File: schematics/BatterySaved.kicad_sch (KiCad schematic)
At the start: 11 parts, among them Q1 2SA1015, Q2 2SC1815, U2 74LS32

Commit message: WIP
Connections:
- net BATYCC renamed BATV_CC
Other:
- note added: "14 pin: BAT_VCC"
- note removed: "14 pin: BATYCC"
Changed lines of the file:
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@@
     (fill (type none))
   )
-  (text "14 pin: BATYCC" (at 82.55 87.63 0)
+  (text "14 pin: BAT_VCC" (at 82.55 87.63 0)
     (effects (font (size 1.27 1.27)) (justify left bottom))
   )
@@
     )
   )
-  (global_label "BATYCC" (shape input) (at 102.87 46.99 0) (fields_autoplaced)
+  (global_label "BATV_CC" (shape output) (at 102.87 46.99 0) (fields_autoplaced)
     (effects (font (size 1.27 1.27)) (justify left))
-    (property "Intersheetrefs" "${INTERSHEET_REFS}" (at 112.81 46.99 0)
+    (property "Intersheetrefs" "${INTERSHEET_REFS}" (at 113.7776 46.99 0)
       (effects (font (size 1.27 1.27)) (justify left))
     )

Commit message: Complete pages 1-4
completion of pages 1 to 4
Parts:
- R1, R2, R3, R4: symbol Device:R_Small_US -> Device:R
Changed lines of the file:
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@@
     (comment 4 "NEO-GEO MVS MV1F")
   )
+  (junction (at 62.23 57.15) (diameter 0) (color 0 0 0 0)
+  )
   (junction (at 54.61 101.6) (diameter 0) (color 0 0 0 0)
   )
@@
   (junction (at 41.91 39.37) (diameter 0) (color 0 0 0 0)
   )
-  (junction (at 62.23 57.15) (diameter 0) (color 0 0 0 0)
-  )
   (junction (at 87.63 46.99) (diameter 0) (color 0 0 0 0)
   )
@@
     (stroke (width 0) (type default))
   )
-  (wire (pts (xy 72.39 46.99) (xy 72.39 49.53))
+  (wire (pts (xy 72.39 46.99) (xy 72.39 48.26))
     (stroke (width 0) (type default))
   )
@@
     (stroke (width 0) (type default))
   )
-  (wire (pts (xy 59.69 83.82) (xy 29.21 83.82))
+  (wire (pts (xy 29.21 83.82) (xy 58.42 83.82))
     (stroke (width 0) (type default))
   )
@@
     (stroke (width 0) (type default))
   )
-  (wire (pts (xy 41.91 39.37) (xy 45.72 39.37))
-    (stroke (width 0) (type default))
-  )
   (wire (pts (xy 73.66 113.03) (xy 76.2 113.03))
     (stroke (width 0) (type default))
   )
+  (wire (pts (xy 62.23 57.15) (xy 62.23 55.88))
+    (stroke (width 0) (type default))
+  )
   (wire (pts (xy 45.72 110.49) (xy 58.42 110.49))
     (stroke (width 0) (type default))
   )
+  (wire (pts (xy 87.63 46.99) (xy 72.39 46.99))
+    (stroke (width 0) (type default))
+  )
+  (wire (pts (xy 58.42 96.52) (xy 54.61 96.52))
+    (stroke (width 0) (type default))
+  )
+  (wire (pts (xy 76.2 99.06) (xy 83.82 99.06))
+    (stroke (width 0) (type default))
+  )
+  (wire (pts (xy 58.42 140.97) (xy 52.07 140.97))
+    (stroke (width 0) (type default))
+  )
+  (wire (pts (xy 73.66 129.54) (xy 83.82 129.54))
+    (stroke (width 0) (type default))
+  )
+  (wire (pts (xy 45.72 115.57) (xy 58.42 115.57))
+    (stroke (width 0) (type default))
+  )
+  (wire (pts (xy 41.91 39.37) (xy 41.91 46.99))
+    (stroke (width 0) (type default))
+  )
+  (wire (pts (xy 29.21 83.82) (xy 29.21 60.96))
+    (stroke (width 0) (type default))
+  )
+  (wire (pts (xy 52.07 39.37) (xy 54.61 39.37))
+    (stroke (width 0) (type default))
+  )
+  (wire (pts (xy 54.61 101.6) (xy 58.42 101.6))
+    (stroke (width 0) (type default))
+  )
+  (wire (pts (xy 76.2 120.65) (xy 52.07 120.65))
+    (stroke (width 0) (type default))
+  )
+  (wire (pts (xy 45.72 101.6) (xy 54.61 101.6))
+    (stroke (width 0) (type default))
+  )
+  (wire (pts (xy 87.63 46.99) (xy 87.63 59.69))
+    (stroke (width 0) (type default))
+  )
+  (wire (pts (xy 76.2 83.82) (xy 76.2 99.06))
+    (stroke (width 0) (type default))
+  )
   (wire (pts (xy 62.23 57.15) (xy 62.23 58.42))
     (stroke (width 0) (type default))
   )
-  (wire (pts (xy 87.63 46.99) (xy 72.39 46.99))
-    (stroke (width 0) (type default))
-  )
-  (wire (pts (xy 62.23 55.88) (xy 62.23 57.15))
-    (stroke (width 0) (type default))
-  )
-  (wire (pts (xy 58.42 96.52) (xy 54.61 96.52))
-    (stroke (width 0) (type default))
-  )
-  (wire (pts (xy 76.2 99.06) (xy 83.82 99.06))
-    (stroke (width 0) (type default))
-  )
-  (wire (pts (xy 58.42 140.97) (xy 52.07 140.97))
-    (stroke (width 0) (type default))
-  )
-  (wire (pts (xy 73.66 129.54) (xy 83.82 129.54))
-    (stroke (width 0) (type default))
-  )
-  (wire (pts (xy 45.72 115.57) (xy 58.42 115.57))
-    (stroke (width 0) (type default))
-  )
-  (wire (pts (xy 41.91 39.37) (xy 41.91 46.99))
-    (stroke (width 0) (type default))
-  )
-  (wire (pts (xy 29.21 83.82) (xy 29.21 60.96))
-    (stroke (width 0) (type default))
-  )
-  (wire (pts (xy 50.8 39.37) (xy 54.61 39.37))
-    (stroke (width 0) (type default))
-  )
-  (wire (pts (xy 54.61 101.6) (xy 58.42 101.6))
-    (stroke (width 0) (type default))
-  )
-  (wire (pts (xy 76.2 120.65) (xy 52.07 120.65))
-    (stroke (width 0) (type default))
-  )
-  (wire (pts (xy 45.72 101.6) (xy 54.61 101.6))
-    (stroke (width 0) (type default))
-  )
-  (wire (pts (xy 87.63 46.99) (xy 87.63 59.69))
-    (stroke (width 0) (type default))
-  )
-  (wire (pts (xy 76.2 83.82) (xy 76.2 99.06))
-    (stroke (width 0) (type default))
-  )
   (wire (pts (xy 52.07 140.97) (xy 52.07 127))
     (stroke (width 0) (type default))
@@
     (stroke (width 0) (type default))
   )
-  (wire (pts (xy 50.8 46.99) (xy 62.23 46.99))
+  (wire (pts (xy 52.07 46.99) (xy 62.23 46.99))
     (stroke (width 0) (type default))
   )
@@
     (stroke (width 0) (type default))
   )
-  (wire (pts (xy 41.91 46.99) (xy 45.72 46.99))
+  (wire (pts (xy 41.91 39.37) (xy 44.45 39.37))
+    (stroke (width 0) (type default))
+  )
+  (wire (pts (xy 41.91 46.99) (xy 44.45 46.99))
     (stroke (width 0) (type default))
   )
@@
     (stroke (width 0) (type default))
   )
-  (wire (pts (xy 76.2 83.82) (xy 64.77 83.82))
+  (wire (pts (xy 76.2 83.82) (xy 66.04 83.82))
     (stroke (width 0) (type default))
   )
@@
     (stroke (width 0) (type default))
   )
-  (wire (pts (xy 62.23 46.99) (xy 62.23 50.8))
+  (wire (pts (xy 62.23 46.99) (xy 62.23 48.26))
+    (stroke (width 0) (type default))
+  )
+  (wire (pts (xy 72.39 57.15) (xy 72.39 55.88))
     (stroke (width 0) (type default))
   )
@@
     )
   )
-  (symbol (lib_id "Device:R_Small_US") (at 62.23 53.34 180) (unit 1)
-    (in_bom yes) (on_board yes) (dnp no) (fields_autoplaced)
-    (property "Reference" "R3" (at 57.1967 53.34 90)
-      (effects (font (size 1.27 1.27)) hide)
-    )
-    (property "Value" "470" (at 63.881 53.34 0)
+  (symbol (lib_id "Device:R") (at 62.23 52.07 180) (unit 1)
+    (in_bom yes) (on_board yes) (dnp no) (fields_autoplaced)
+    (property "Reference" "R3" (at 57.1967 52.07 90)
+      (effects (font (size 1.27 1.27)) hide)
+    )
+    (property "Value" "470" (at 63.881 52.07 0)
       (effects (font (size 1.27 1.27)) (justify right))
     )
-    (property "Footprint" "" (at 62.23 53.34 0)
-      (effects (font (size 1.27 1.27)) hide)
-    )
-    (property "Datasheet" "~" (at 62.23 53.34 0)
+    (property "Footprint" "" (at 64.008 52.07 90)
+      (effects (font (size 1.27 1.27)) hide)
+    )
+    (property "Datasheet" "~" (at 62.23 52.07 0)
       (effects (font (size 1.27 1.27)) hide)
     )
@@
     )
   )
-  (symbol (lib_id "Device:R_Small_US") (at 62.23 83.82 90) (unit 1)
+  (symbol (lib_id "Device:R") (at 62.23 83.82 90) (unit 1)
     (in_bom yes) (on_board yes) (dnp no) (fields_autoplaced)
     (property "Reference" "R4" (at 62.23 78.7867 90)
@@
       (effects (font (size 1.27 1.27)))
     )
-    (property "Footprint" "" (at 62.23 83.82 0)
+    (property "Footprint" "" (at 62.23 85.598 90)
       (effects (font (size 1.27 1.27)) hide)
     )
@@
     )
   )
-  (symbol (lib_id "Diode:1N4001") (at 72.39 53.34 270) (unit 1)
-    (in_bom yes) (on_board yes) (dnp no) (fields_autoplaced)
-    (property "Reference" "D2" (at 70.358 54.5521 90)
+  (symbol (lib_id "Diode:1N4001") (at 72.39 52.07 270) (unit 1)
+    (in_bom yes) (on_board yes) (dnp no) (fields_autoplaced)
+    (property "Reference" "D2" (at 70.358 53.2821 90)
       (effects (font (size 1.27 1.27)) (justify right) hide)
     )
-    (property "Value" "1S1588" (at 74.422 53.34 90)
-      (effects (font (size 1.27 1.27)) (justify left))
-    )
-    (property "Footprint" "Diode_THT:D_DO-41_SOD81_P10.16mm_Horizontal" (at 72.39 53.34 0)
-      (effects (font (size 1.27 1.27)) hide)
-    )
-    (property "Datasheet" "http://www.vishay.com/docs/88503/1n4001.pdf" (at 72.39 53.34 0)
-      (effects (font (size 1.27 1.27)) hide)
-    )
-    (property "Sim.Device" "D" (at 72.39 53.34 0)
-      (effects (font (size 1.27 1.27)) hide)
-    )
-    (property "Sim.Pins" "1=K 2=A" (at 72.39 53.34 0)
+    (property "Value" "1S1588" (at 74.422 52.07 90)
+      (effects (font (size 1.27 1.27)) (justify left))
+    )
+    (property "Footprint" "Diode_THT:D_DO-41_SOD81_P10.16mm_Horizontal" (at 72.39 52.07 0)
+      (effects (font (size 1.27 1.27)) hide)
+    )
+    (property "Datasheet" "http://www.vishay.com/docs/88503/1n4001.pdf" (at 72.39 52.07 0)
+      (effects (font (size 1.27 1.27)) hide)
+    )
+    (property "Sim.Device" "D" (at 72.39 52.07 0)
+      (effects (font (size 1.27 1.27)) hide)
+    )
+    (property "Sim.Pins" "1=K 2=A" (at 72.39 52.07 0)
       (effects (font (size 1.27 1.27)) hide)
     )
@@
     )
   )
-  (symbol (lib_id "Device:R_Small_US") (at 48.26 39.37 90) (unit 1)
+  (symbol (lib_id "Device:R") (at 48.26 39.37 90) (unit 1)
     (in_bom yes) (on_board yes) (dnp no) (fields_autoplaced)
     (property "Reference" "R1" (at 48.26 34.3367 90)
@@
       (effects (font (size 1.27 1.27)))
     )
-    (property "Footprint" "" (at 48.26 39.37 0)
+    (property "Footprint" "" (at 48.26 41.148 90)
       (effects (font (size 1.27 1.27)) hide)
     )
@@
     )
   )
-  (symbol (lib_id "Device:R_Small_US") (at 48.26 46.99 90) (unit 1)
+  (symbol (lib_id "Device:R") (at 48.26 46.99 90) (unit 1)
     (in_bom yes) (on_board yes) (dnp no) (fields_autoplaced)
     (property "Reference" "R2" (at 48.26 41.9567 90)
@@
       (effects (font (size 1.27 1.27)))
     )
-    (property "Footprint" "" (at 48.26 46.99 0)
-      (effects (font (size 1.27 1.27)) hide)
-    )
+    (property "Footprint" "" (at 48.26 48.768 90)
+      (effects (font (size 1.27 1.27)) hide)
+    )

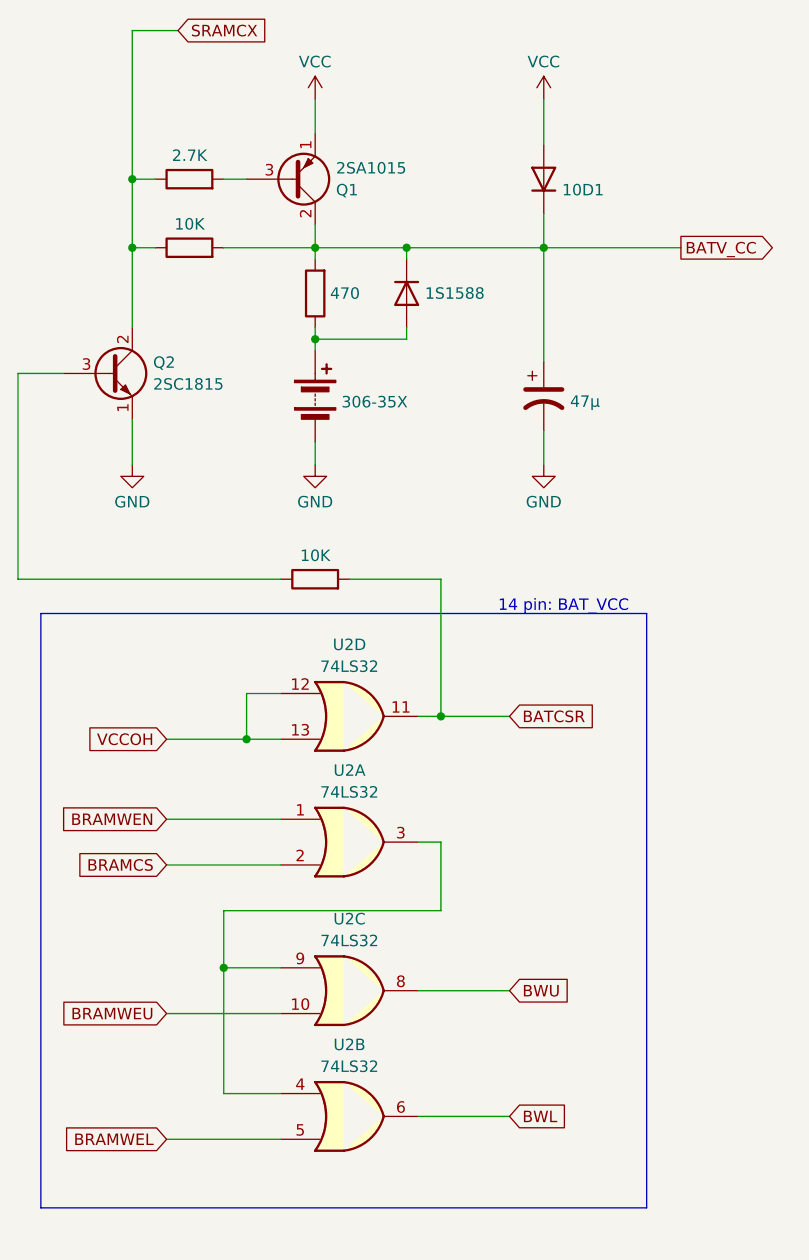
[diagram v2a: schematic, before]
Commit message: Audio Amp + player's button LED & marquee + Coins Up + 45% raiser card connectors
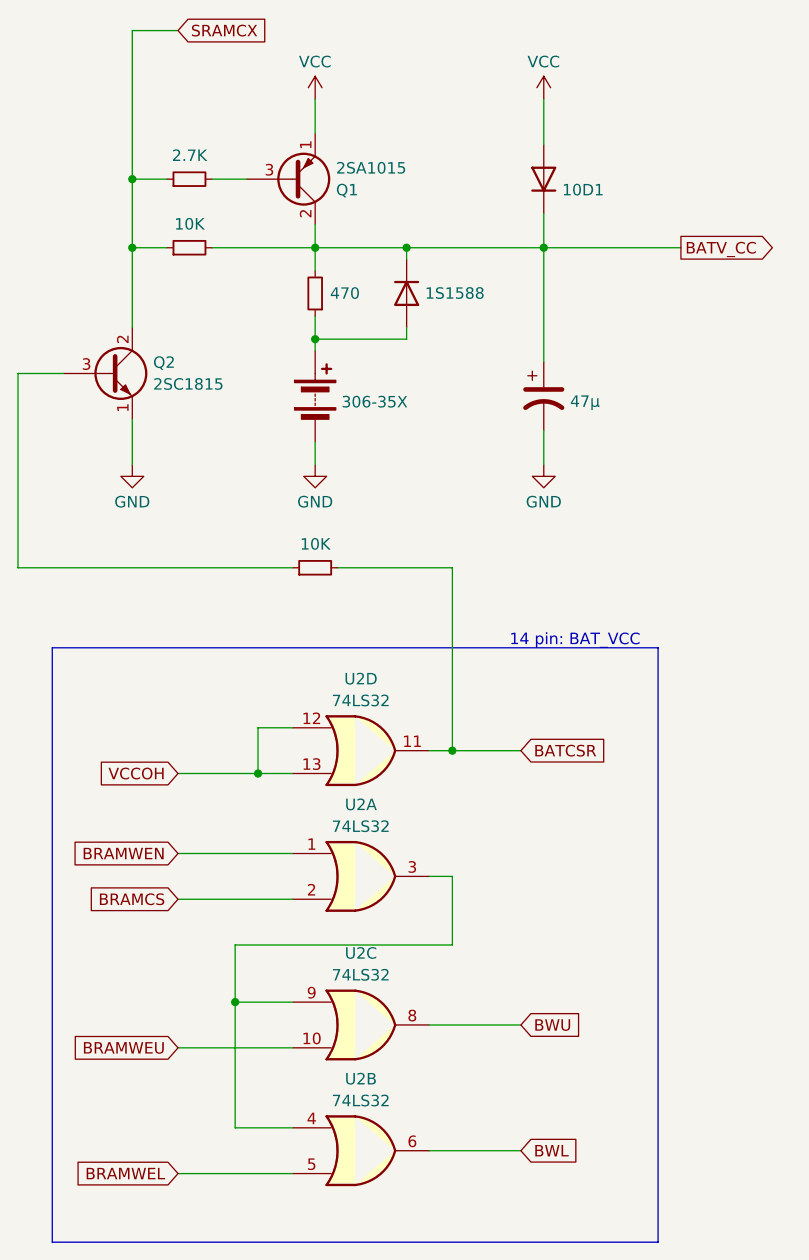
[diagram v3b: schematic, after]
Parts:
- R1, R2, R3, R4: symbol Device:R -> Device:R_Small
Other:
- moved on the sheet: U2A, U2B, U2C, U2D

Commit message: typos
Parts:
- U2: footprint (none) -> Package_DIP:DIP-14_W7.62mm
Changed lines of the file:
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@@
     (comment 3 "Converted by Frater ")
     (comment 4 "NEO-GEO MVS MV1F")
+    (comment 9 "https://github.com/Neo-Geo-Hardwares/Schematics-MV1F")
   )
   (junction (at 62.23 57.15) (diameter 0) (color 0 0 0 0)
@@
       (effects (font (size 1.27 1.27)))
     )
-    (property "Footprint" "" (at 67.31 102.87 0)
+    (property "Footprint" "Package_DIP:DIP-14_W7.62mm" (at 67.31 102.87 0)
       (effects (font (size 1.27 1.27)) hide)
     )
@@
       (effects (font (size 1.27 1.27)))
     )
-    (property "Footprint" "" (at 67.31 116.84 0)
+    (property "Footprint" "Package_DIP:DIP-14_W7.62mm" (at 67.31 116.84 0)
       (effects (font (size 1.27 1.27)) hide)
     )
@@
       (effects (font (size 1.27 1.27)))
     )
-    (property "Footprint" "" (at 67.31 133.35 0)
+    (property "Footprint" "Package_DIP:DIP-14_W7.62mm" (at 67.31 133.35 0)
       (effects (font (size 1.27 1.27)) hide)
     )
@@
       (effects (font (size 1.27 1.27)))
     )
-    (property "Footprint" "" (at 67.31 147.32 0)
-      (effects (font (size 1.27 1.27)) hide)
-    )
+    (property "Footprint" "Package_DIP:DIP-14_W7.62mm" (at 67.31 147.32 0)
+      (effects (font (size 1.27 1.27)) hide)
+    )
